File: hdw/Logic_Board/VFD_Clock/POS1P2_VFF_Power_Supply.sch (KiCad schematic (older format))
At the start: 23 parts

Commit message: Added display board schematic, other additions to logic board
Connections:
- wire segments 68 -> 69
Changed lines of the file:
@@
 $Descr A 11000 8500
 encoding utf-8
-Sheet 5 19
+Sheet 4 21
 Title "VFD Clock"
 Date "2019-04-11"
@@
 Wire Wire Line
 	6640 4230 6030 4230
-Wire Wire Line
-	6640 3530 6640 3230
-Wire Wire Line
-	6030 3230 6030 3530
-Connection ~ 6030 3230
-Wire Wire Line
-	6030 3230 5820 3230
 Connection ~ 6030 4230
 Wire Wire Line
@@
 	8080 3230 8080 3290
 Connection ~ 7440 3230
-Wire Wire Line
-	6030 3230 6640 3230
-Connection ~ 6640 3230
-Wire Wire Line
-	6640 3230 7440 3230
 $Comp
 L Custom_Library:C_Custom C?
@@
 	1    9180 3900
 	0    -1   1    0
-$EndComp
-$Comp
-L Custom_Library:R_Custom R?
-U 1 1 5CB29476
-P 8880 3230
-AR Path="/5CB364CC/5CB29476" Ref="R?"  Part="1"
-AR Path="/5A0A7E5F/5CB29476" Ref="R?"  Part="1"
-F 0 "R?" V 8780 3230 50  0000 C CNN
-F 1 "0.02" V 8880 3230 40  0000 C CNN
-F 2 "Resistors_SMD:R_0612" H 8880 3230 50  0001 C CNN
-F 3 "" H 8880 3230 50  0001 C CNN
-F 4 "P16010CT-ND" H 9180 3630 60  0001 C CNN "Digi-Key PN"
-F 5 "0612" V 8980 3230 50  0000 C CNN "display_footprint"
-F 6 "1%" V 9080 3230 50  0000 C CNN "Tolerance"
-F 7 "1W" V 9180 3230 50  0000 C CNN "Wattage"
-	1    8880 3230
-	0    -1   -1   0
 $EndComp
 Wire Wire Line
@@
 	1    0    0    -1
 $EndComp
-Text Notes 9030 5190 0    50   ~ 0
-1.996 V/A
+Wire Wire Line
+	5820 3230 7440 3230
+Wire Wire Line
+	9110 3230 9110 2820
+Wire Wire Line
+	9110 2820 6640 2820
+Wire Wire Line
+	6030 2820 6030 3530
+Wire Wire Line
+	6640 3530 6640 2820
+Connection ~ 6640 2820
+Wire Wire Line
+	6640 2820 6030 2820
+$Comp
+L Custom_Library:R_Custom R?
+U 1 1 5CB29476
+P 8880 3230
+AR Path="/5CB364CC/5CB29476" Ref="R?"  Part="1"
+AR Path="/5A0A7E5F/5CB29476" Ref="R?"  Part="1"
+F 0 "R?" V 8780 3230 50  0000 C CNN
+F 1 "0.02" V 8880 3230 40  0000 C CNN
+F 2 "Resistors_SMD:R_0612" H 8880 3230 50  0001 C CNN
+F 3 "" H 8880 3230 50  0001 C CNN
+F 4 "P16010CT-ND" H 9180 3630 60  0001 C CNN "Digi-Key PN"
+F 5 "0612" V 8980 3230 50  0000 C CNN "display_footprint"
+F 6 "1%" V 9080 3230 50  0000 C CNN "Tolerance"
+F 7 "1W" V 9180 3230 50  0000 C CNN "Wattage"
+	1    8880 3230
+	0    -1   -1   0
+$EndComp
 $EndSCHEMATC

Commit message: Resurrected project
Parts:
- removed C?: 15pF, Capacitors_SMD:C_0603, symbol Custom_Library:C_Custom
- removed C?: 2.2uF, Capacitors_SMD:C_0805, symbol Custom_Library:C_Custom
- removed C? (x3): 0.1uF, Capacitors_SMD:C_0603, symbol Custom_Library:C_Custom
- removed C?: 47uF, Capacitors_SMD:C_1206, symbol Custom_Library:C_Custom
- removed C?: 47uF, Capacitors_SMD:C_1210, symbol Custom_Library:C_Custom
- removed C?: 47uF, Capacitors_Tantalum_SMD:CP_Tantalum_Case-B_EIA-3528-21_Reflow, symbol Custom_Library:CP_Tant_Custom
- removed C? (x2): 1nF, Capacitors_SMD:C_0603, symbol Custom_Library:C_Custom
- removed C?: 10nF, Capacitors_SMD:C_0603, symbol Custom_Library:C_Custom
- removed L?: 0.47uH, Inductors_SMD:L_Vishay_IHLP-1212, symbol Custom_Library:L_Custom
- removed R? (x2): 619k, Resistors_SMD:R_0603, symbol Custom_Library:R_Custom
- removed R? (x4): 10k, Resistors_SMD:R_0603, symbol Custom_Library:R_Custom
- removed R?: 0.02, Resistors_SMD:R_0612, symbol Custom_Library:R_Custom
- removed R?: 499k, Resistors_SMD:R_0603, symbol Custom_Library:R_Custom
- removed TP?: TP, Custom Footprints Library:Test_Point, symbol Custom_Library:TP
- removed U?: LTC3624DD, Housings_DFN_QFN:DFN-8-1EP_3x3mm_Pitch0.5mm, symbol Custom_Library:LTC3624DD
- removed U?: INA138, TO_SOT_Packages_SMD:SOT-23-5, symbol Amplifier_Current:INA138
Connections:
- net labels removed: +1.2V_VFF, +3.3V, GND, POS1P2_VFF_ISNS, POS1P2_VFF_PGOOD, POS1P2_VFF_RUN
- wire segments 69 -> 0
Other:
- note removed: "Designed for 2A Maximum"

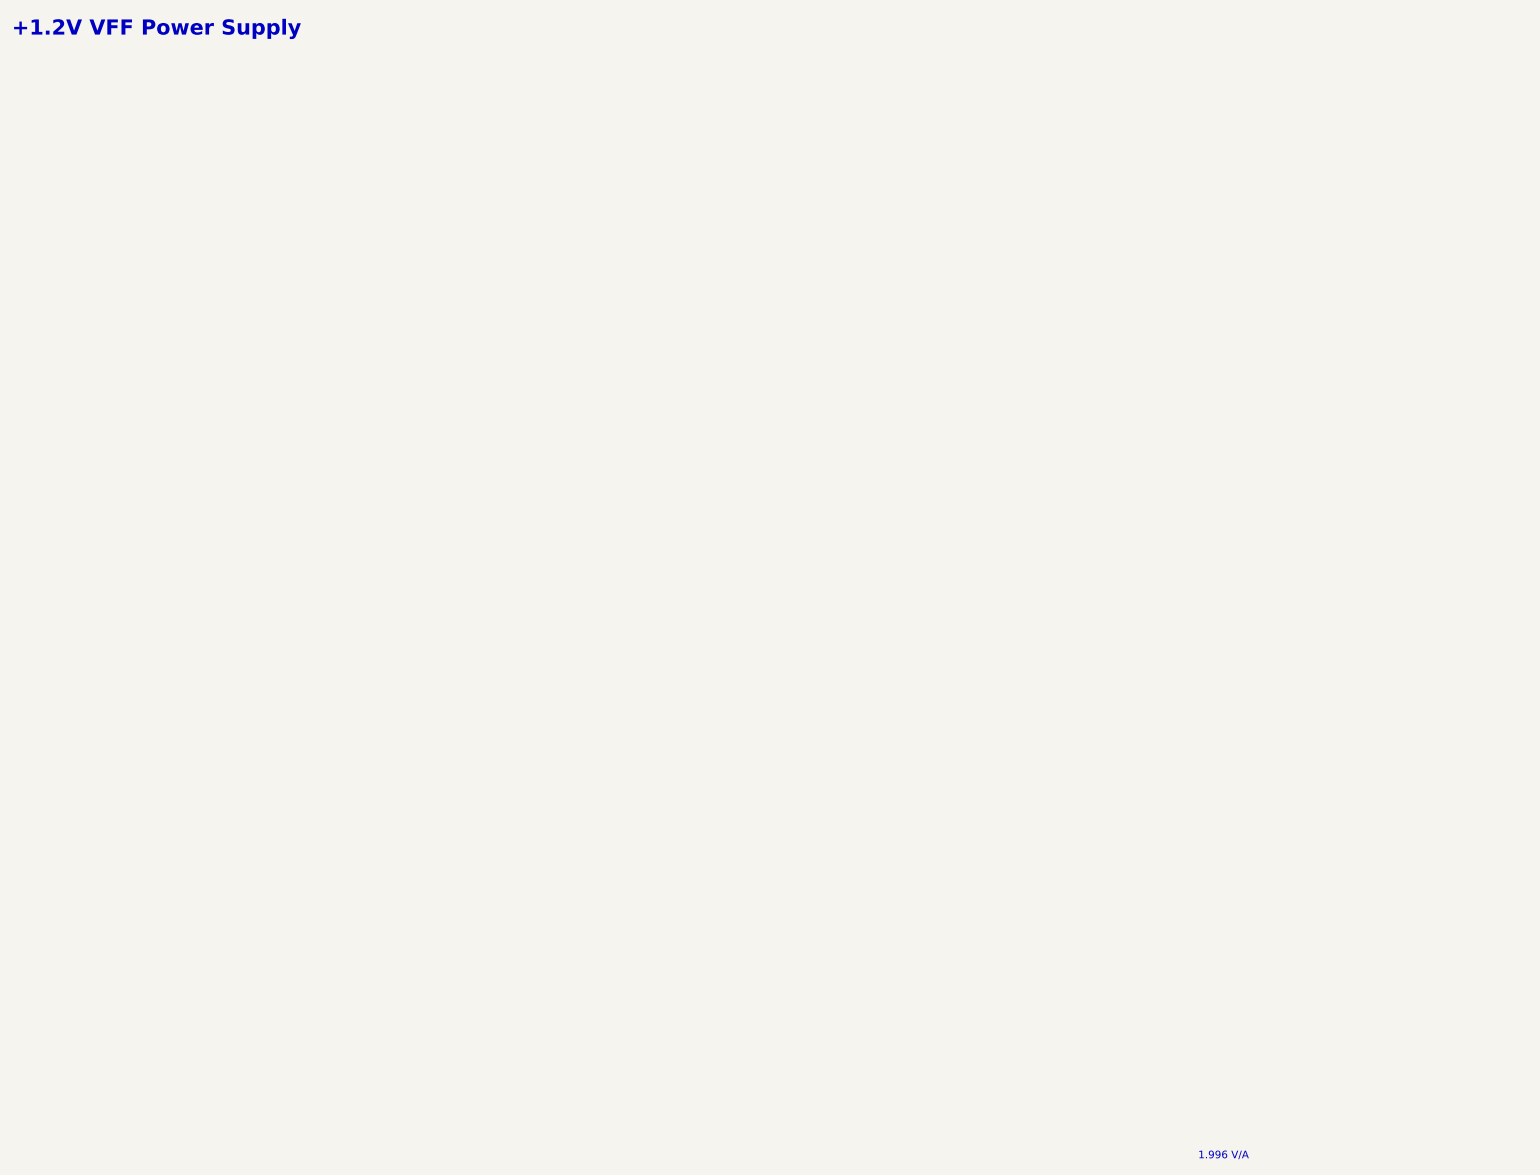
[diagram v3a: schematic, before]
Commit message: Power supply additions
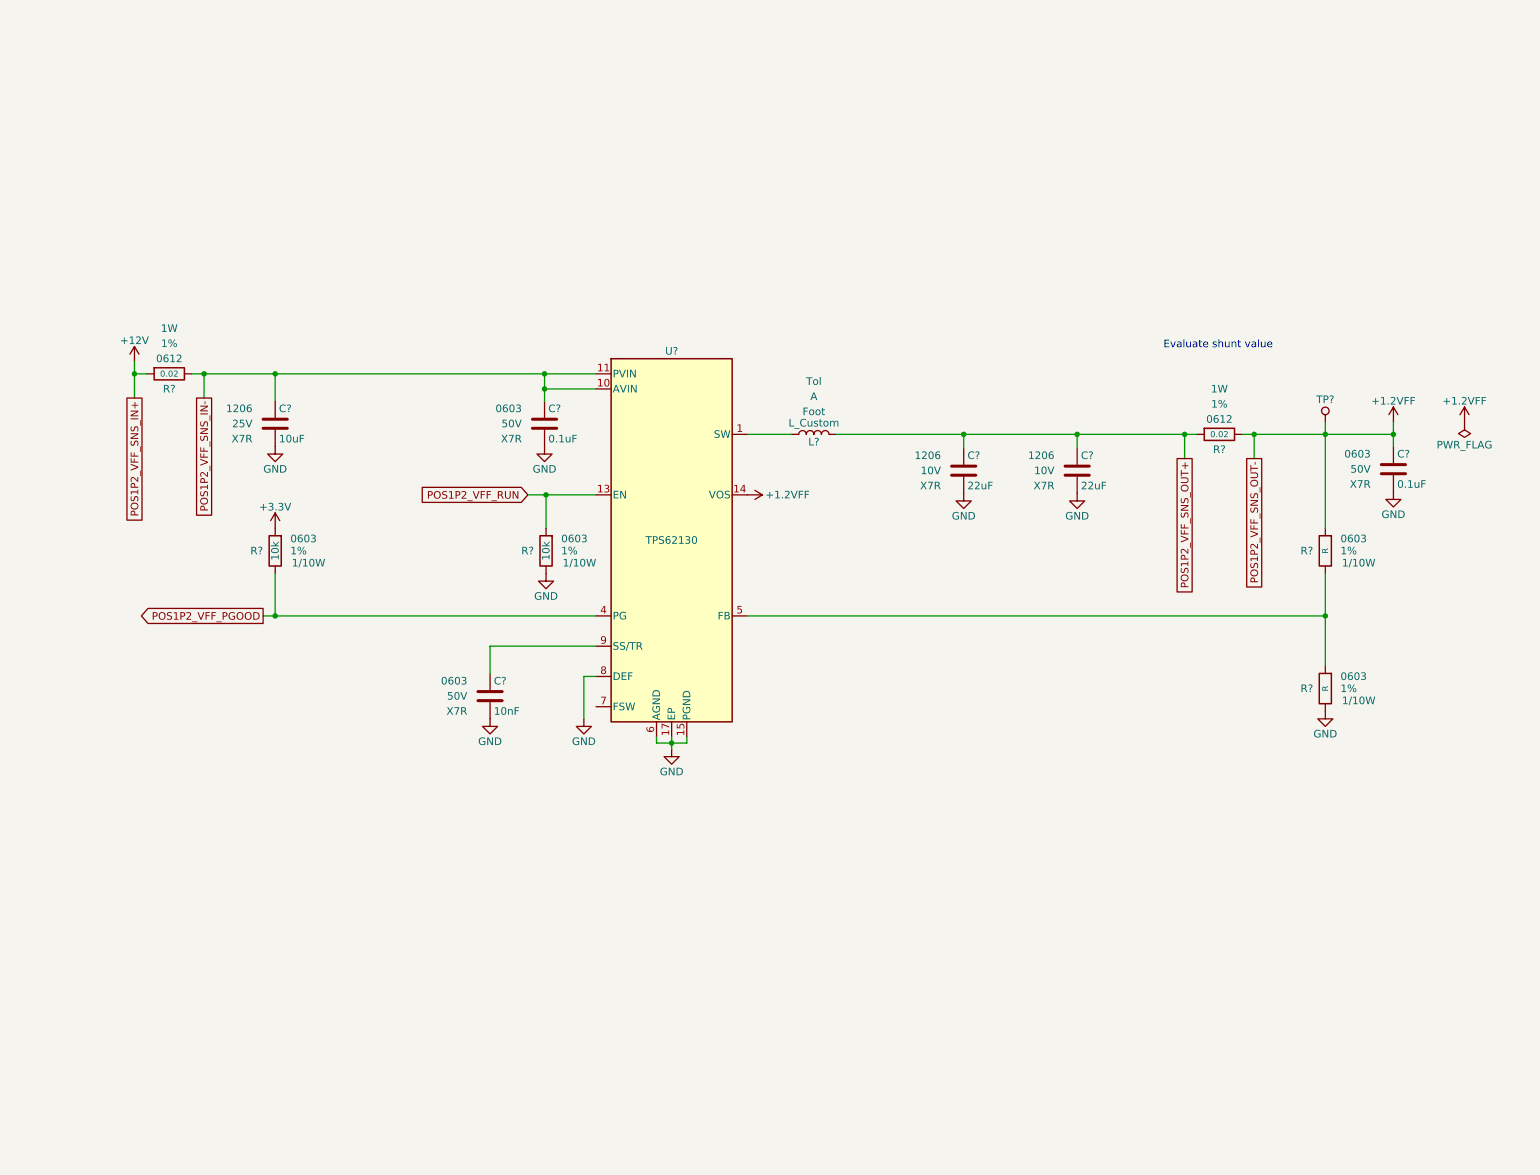
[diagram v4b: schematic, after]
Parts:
- added C? (x2): 0.1uF, Capacitors_SMD:C_0603, symbol Custom_Library:C_Custom
- added C?: 10uF, Capacitors_SMD:C_1206, symbol Custom_Library:C_Custom
- added C? (x2): 22uF, Capacitors_SMD:C_1206, symbol Custom_Library:C_Custom
- added C?: 10nF, Capacitors_SMD:C_0603, symbol Custom_Library:C_Custom
- added L?: L_Custom, symbol Custom_Library:L_Custom
- added R? (x2): 10k, Resistors_SMD:R_0603, symbol Custom_Library:R_Custom
- added R? (x2): 0.02, Resistors_SMD:R_0612, symbol Custom_Library:R_Custom
- added R? (x2): R, Resistors_SMD:R_0603, symbol Custom_Library:R_Custom
- added TP?: TP, Custom Footprints Library:Test_Point, symbol Custom_Library:TP
- added U?: TPS62130, Housings_DFN_QFN:QFN-16-1EP_3x3mm_Pitch0.5mm, symbol Custom_Library:TPS62130
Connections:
- new net: L?.1, U?.1 (SW), U?.2 (SW), U?.3 (SW)
- new net: R?.1, R?.2, U?.5 (FB)
- new net: C?.1, U?.9 (SS/TR)
- new net +1.2VFF: C?.1, R?.1, R?.2, TP?.1 (TP), U?.14 (VOS)
- new net +12V: R?.1
- new net +3V3: R?.1
- new net GND: C?.2, C?.2, C?.2, C?.2, C?.2, C?.2, R?.2, R?.2, U?.15 (PGND), U?.16 (PGND), U?.17 (EP), U?.6 (AGND), U?.8 (DEF)
- new net POS1P2_VFF_PGOOD: R?.2, U?.4 (PG)
- new net POS1P2_VFF_RUN: R?.1, U?.13 (EN)
- new net POS1P2_VFF_SNS_IN-: C?.1, C?.1, R?.2, U?.10 (AVIN), U?.11 (PVIN), U?.12 (PVIN)
- new net POS1P2_VFF_SNS_OUT+: C?.1, C?.1, L?.2, R?.1
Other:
- note added: "Evaluate shunt value"
- note removed: "+1.2V VFF Power Supply"
- note removed: "1.996 V/A"

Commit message: Changed to configurable discrete gates, added VBAT stuff
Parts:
- removed C?: 0.1uF, Capacitors_SMD:C_0603, symbol Custom_Library:C_Custom
- removed C?: 10uF, Capacitors_SMD:C_1206, symbol Custom_Library:C_Custom
- removed C? (x2): 22uF, Capacitors_SMD:C_1206, symbol Custom_Library:C_Custom
- removed C?: 10nF, Capacitors_SMD:C_0603, symbol Custom_Library:C_Custom
- removed R?: 0.02, Resistors_SMD:R_0612, symbol Custom_Library:R_Custom
- removed R?: R, Resistors_SMD:R_0603, symbol Custom_Library:R_Custom
- removed TP?: TP, Custom Footprints Library:Test_Point, symbol Custom_Library:TP
- removed U?: TPS62130, Housings_DFN_QFN:QFN-16-1EP_3x3mm_Pitch0.5mm, symbol Custom_Library:TPS62130
- added C?: 0.1uF, Capacitors_SMD:C_0603, symbol Custom_Library:C_Custom
- added C?: 10uF, Capacitors_SMD:C_1206, symbol Custom_Library:C_Custom
- added C? (x2): 22uF, Capacitors_SMD:C_1206, symbol Custom_Library:C_Custom
- added C?: 10nF, Capacitors_SMD:C_0603, symbol Custom_Library:C_Custom
- added R?: 0.02, Resistors_SMD:R_0612, symbol Custom_Library:R_Custom
- added R?: R, Resistors_SMD:R_0603, symbol Custom_Library:R_Custom
- added TP?: TP, Custom Footprints Library:Test_Point, symbol Custom_Library:TP
- added U?: TPS62130, Housings_DFN_QFN:QFN-16-1EP_3x3mm_Pitch0.5mm, symbol Custom_Library:TPS62130
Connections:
- net +1.2VFF: now also R?.1, R?.2, TP?.1 (TP), U?.14 (VOS)
- net GND: now also C?.2, C?.2, C?.2, C?.2, C?.2, U?.15 (PGND), U?.16 (PGND), U?.17 (EP), U?.6 (AGND), U?.8 (DEF)
- net POS1P2_VFF_PGOOD: now also U?.4 (PG)
- net POS1P2_VFF_RUN: now also U?.13 (EN)
- net POS1P2_VFF_SNS_IN-: now also C?.1, C?.1, U?.10 (AVIN), U?.11 (PVIN), U?.12 (PVIN)
- net POS1P2_VFF_SNS_OUT+: now also C?.1, C?.1, R?.1
- net at L?.1: now also U?.1 (SW), U?.2 (SW), U?.3 (SW)
- net at R?.1: now also R?.2, U?.5 (FB)
- new net: C?.1, U?.9 (SS/TR)
